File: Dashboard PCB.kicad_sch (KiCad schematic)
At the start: 42 parts

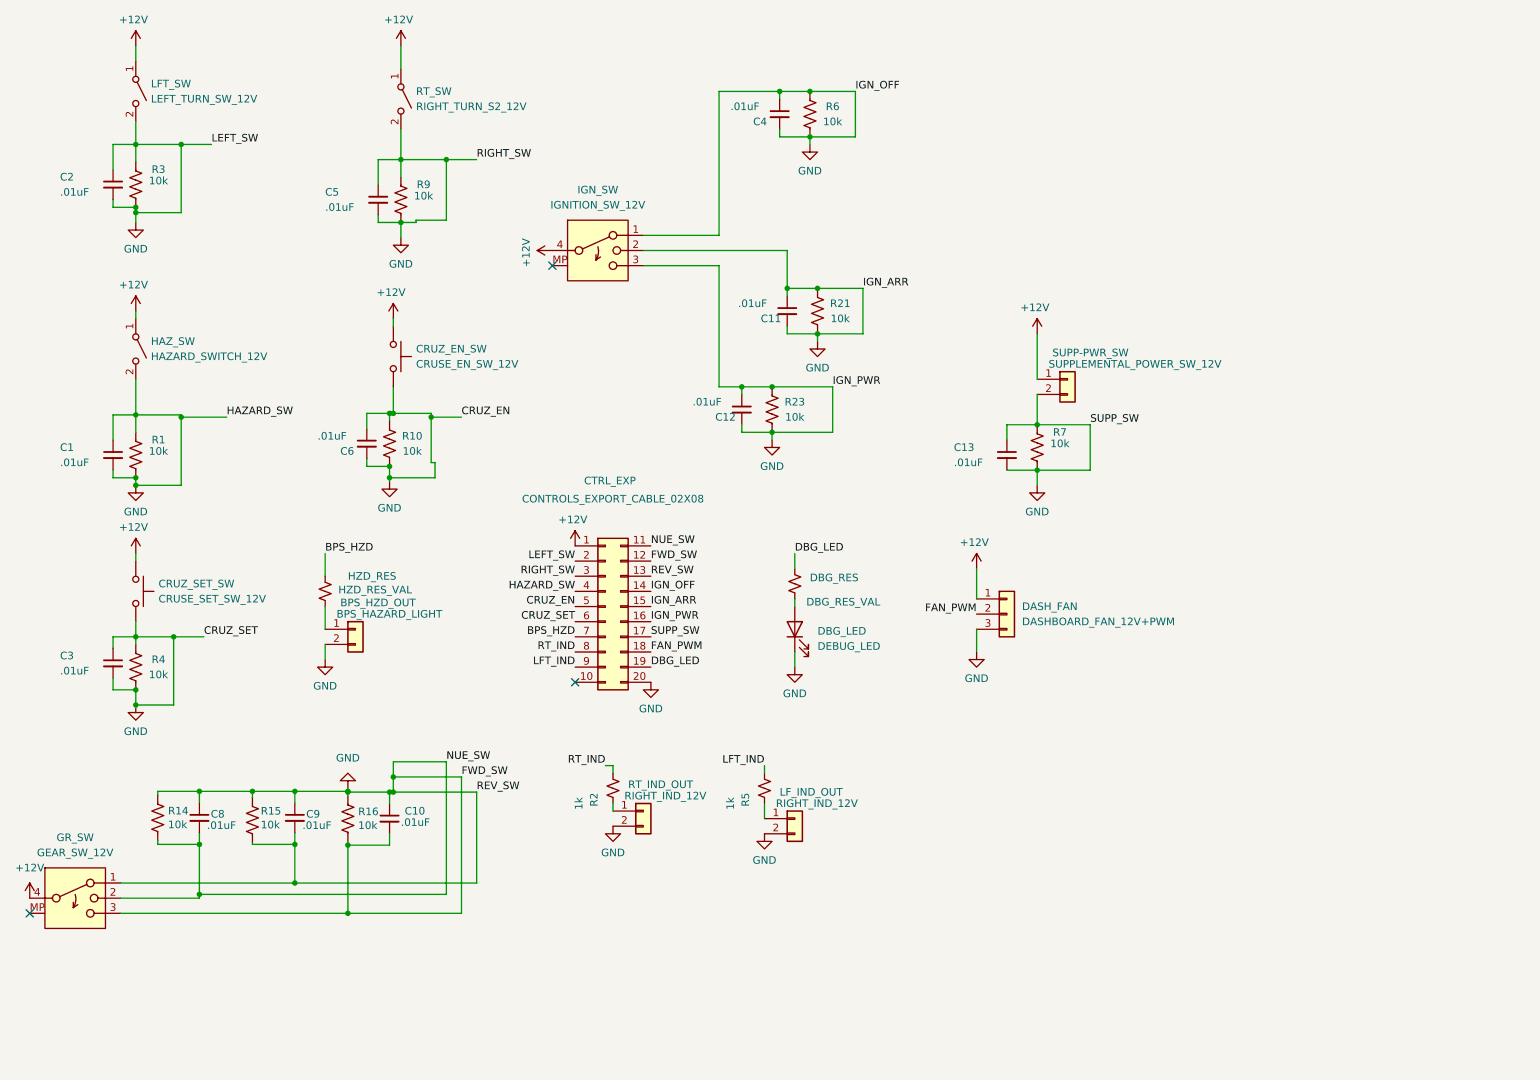
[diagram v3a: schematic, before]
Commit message: Updated dashboard
Took off some unnecessary connections
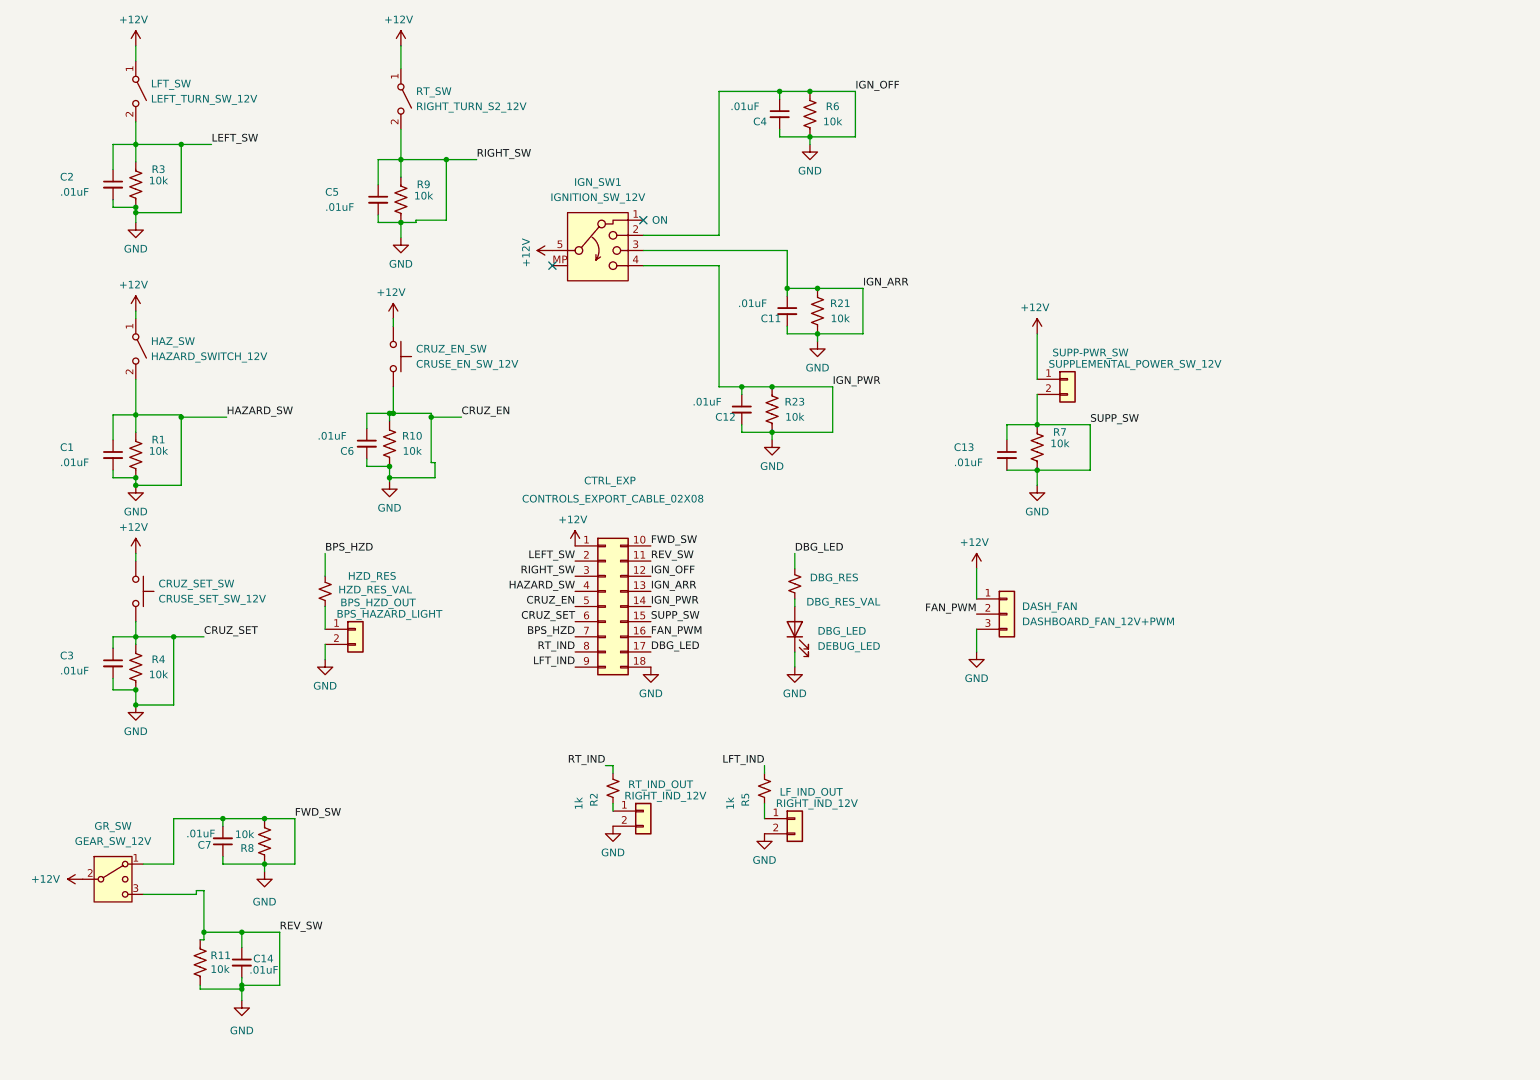
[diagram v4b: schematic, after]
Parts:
- removed C10, C8, C9: .01uF, Capacitor_SMD:C_0805_2012Metric, symbol Device:C_Small
- removed GR_SW: GEAR_SW_12V, symbol Switch:SW_Rotary_1x3_MP
- removed IGN_SW: IGNITION_SW_12V, symbol Switch:SW_Rotary_1x3_MP
- removed R14, R15, R16: 10k, Resistor_SMD:R_0805_2012Metric, symbol Device:R_US
- added C14, C7: .01uF, Capacitor_SMD:C_0805_2012Metric, symbol Device:C_Small
- added GR_SW: GEAR_SW_12V, symbol Switch:SW_SPDT_MSM
- added IGN_SW1: IGNITION_SW_12V, symbol Switch:SW_Rotary_1x4_MP
- added R11, R8: 10k, Resistor_SMD:R_0805_2012Metric, symbol Device:R_US
- CTRL_EXP: symbol Connector_Generic:Conn_02x10_Top_Bottom -> Connector_Generic:Conn_02x09_Top_Bottom
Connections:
- net +12V: now also GR_SW.2 (3), IGN_SW1.5
- net DBG_LED: now also CTRL_EXP.17 (Pin_17); no longer CTRL_EXP.19 (Pin_19)
- net FAN_PWM: now also CTRL_EXP.16 (Pin_16); no longer CTRL_EXP.18 (Pin_18)
- net GND: now also CTRL_EXP.10 (Pin_10), CTRL_EXP.18 (Pin_18), C14.1, C14.2, C7.1, C7.2, GR_SW.1, GR_SW.3 (4), IGN_SW1.2, IGN_SW1.3, IGN_SW1.4, R11.1, R11.2, R8.1, R8.2; no longer CTRL_EXP.16 (Pin_16), CTRL_EXP.17 (Pin_17), CTRL_EXP.20 (Pin_20)
- no-connect marks 3 -> 2
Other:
- note added: "ON"

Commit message: Major redisign
Added a lot of stuff and redesigned a lot of stuff
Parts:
- removed BPS_HZD_OUT: BPS_HAZARD_LIGHT, Connector_Molex:Molex_Micro-Fit_3.0_43650-0215_1x02_P3.00mm_Vertical, symbol Connector_Generic:Conn_01x02
- removed C1, C11, C14, C2, C3, C4, C5, C6, C7: .01uF, Capacitor_SMD:C_0805_2012Metric, symbol Device:C_Small
- removed CRUZ_EN_SW: CRUSE_EN_SW_12V, symbol Switch:SW_Push
- removed CRUZ_SET_SW: CRUSE_SET_SW_12V, symbol Switch:SW_Push
- removed DASH_FAN: DASHBOARD_FAN_12V+PWM, symbol Connector_Generic:Conn_01x03
- removed DBG_LED: DEBUG_LED, symbol Device:LED
- removed DBG_RES: DBG_RES_VAL, Resistor_SMD:R_0805_2012Metric, symbol Device:R_Small_US
- removed GR_SW: GEAR_SW_12V, symbol Switch:SW_SPDT_MSM
- removed HAZ_SW: HAZARD_SWITCH_12V, symbol Switch:SW_SPST
- removed HZD_RES: HZD_RES_VAL, Resistor_SMD:R_0805_2012Metric, symbol Device:R_Small_US
- removed IGN_SW1: IGNITION_SW_12V, symbol Switch:SW_Rotary_1x4_MP
- removed LFT_SW: LEFT_TURN_SW_12V, symbol Switch:SW_SPST
- removed LF_IND_OUT, RT_IND_OUT: RIGHT_IND_12V, Connector_Molex:Molex_Micro-Fit_3.0_43650-0215_1x02_P3.00mm_Vertical, symbol Connector_Generic:Conn_01x02
- removed R1, R10, R11, R21, R23, R3, R4, R6, R7, R8, R9: 10k, Resistor_SMD:R_0805_2012Metric, symbol Device:R_US
- removed R2, R5: 1k, Resistor_SMD:R_0805_2012Metric, symbol Device:R_Small_US
- removed RT_SW: RIGHT_TURN_S2_12V, symbol Switch:SW_SPST
- removed SUPP-PWR_SW: SUPPLEMENTAL_POWER_SW_12V, Connector_Molex:Molex_Micro-Fit_3.0_43650-0215_1x02_P3.00mm_Vertical, symbol Connector_Generic:Conn_01x02
- added BL1: LM555xM, Package_SO:SOIC-8_3.9x4.9mm_P1.27mm, symbol Timer:LM555xM
- added C9: 10uF, Capacitor_SMD:C_0805_2012Metric, symbol Device:C_Small
- added D1: 6.8V, Diode_SMD:D_0805_2012Metric, symbol Device:D_Zener
- added DASH_FAN1: DASHBOARD_FAN_12V+PWM, symbol Connector_Generic:Conn_01x03
- added DBG_LED1: DEBUG_LED, symbol Device:LED
- added DBG_RES1: DBG_RES_VAL, Resistor_SMD:R_0805_2012Metric, symbol Device:R_Small_US
- added R2: 1k, Resistor_SMD:R_0805_2012Metric, symbol Device:R_Small
- added R5: 10k, Resistor_SMD:R_0805_2012Metric, symbol Device:R_Small
- added TP1: LIGHT_CLK, TestPoint:TestPoint_Pad_1.5x1.5mm, symbol Connector:TestPoint
- C13: value .01uF -> 47uF; P/N C0805C103J5RACTU -> C2012X5R0J476M125AC
- CTRL_EXP: symbol Connector_Generic:Conn_02x09_Top_Bottom -> Connector_Generic:Conn_02x07_Top_Bottom
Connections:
- net +12V: now also BL1.4 (R), BL1.8 (VCC), C9.1, DASH_FAN1.1 (Pin_1), R2.1
- net BPS_HZD: now also CTRL_EXP.6 (Pin_6); no longer CTRL_EXP.7 (Pin_7)
- net DBG_LED: now also CTRL_EXP.7 (Pin_7), DBG_RES1.1; no longer CTRL_EXP.17 (Pin_17)
- net FAN_PWM: now also CTRL_EXP.13 (Pin_13), DASH_FAN1.2 (Pin_2); no longer CTRL_EXP.16 (Pin_16)
- net GND: now also BL1.1 (GND), C9.2, D1.2 (A), DASH_FAN1.3 (Pin_3), DBG_LED1.1 (K); no longer C12.1, C13.1, CTRL_EXP.10 (Pin_10), CTRL_EXP.11 (Pin_11), CTRL_EXP.12 (Pin_12), CTRL_EXP.13 (Pin_13), CTRL_EXP.15 (Pin_15), CTRL_EXP.18 (Pin_18), CTRL_EXP.2 (Pin_2), CTRL_EXP.3 (Pin_3), CTRL_EXP.4 (Pin_4), CTRL_EXP.5 (Pin_5), CTRL_EXP.6 (Pin_6)
- net LFT_IND renamed REV_SW
- net RT_IND renamed FWD_SW
- new net: DBG_LED1.2 (A), DBG_RES1.2
- new net: BL1.7 (DIS), R2.2, R5.2
- new net: BL1.5 (CV), C12.1
- new net CRUZ_EN: CTRL_EXP.4 (Pin_4)
- new net CRUZ_SET: CTRL_EXP.5 (Pin_5)
- new net IGN_ARR: CTRL_EXP.11 (Pin_11)
- new net IGN_PWR: CTRL_EXP.12 (Pin_12)
- new net LFT_LIGHTS_OUT: CTRL_EXP.3 (Pin_3)
- new net LIGHT_CLK: BL1.3 (Q), D1.1 (K), TP1.1
- new net RT_LIGHTS_OUT: CTRL_EXP.2 (Pin_2)
- new net SUPP_SW: CTRL_EXP.10 (Pin_10)
- new net TRIGTHRES: BL1.2 (TR), BL1.6 (THR), C13.1, R5.1
- no-connect marks 2 -> 0
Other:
- added sheet Lighting (Lighting.kicad_sch)
- added sheet Switches (Switches.kicad_sch)
- note added: "555 Timer with Rhigh = 1k, Rlow = 10k, C = 47u: ~358ms high, ~325ms low, @1.459Hz"
- note removed: "ON"

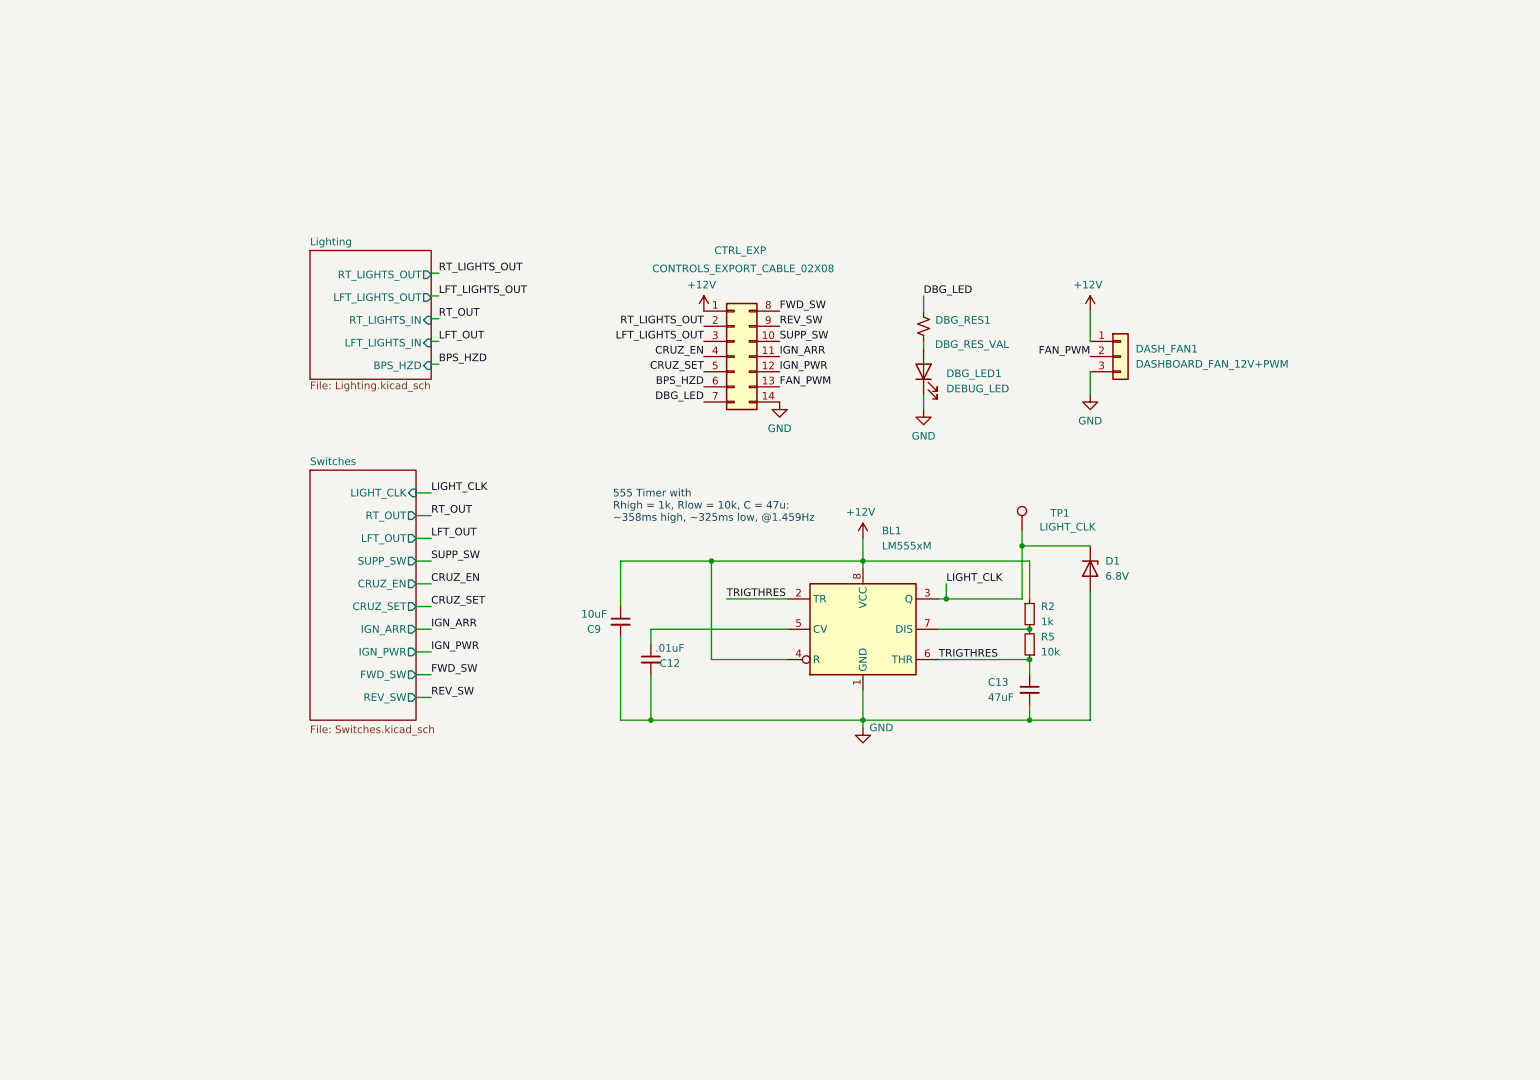
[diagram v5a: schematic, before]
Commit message: Update 1/2
Fixed some of the requested changes.
Still need to fix it up a bit more.
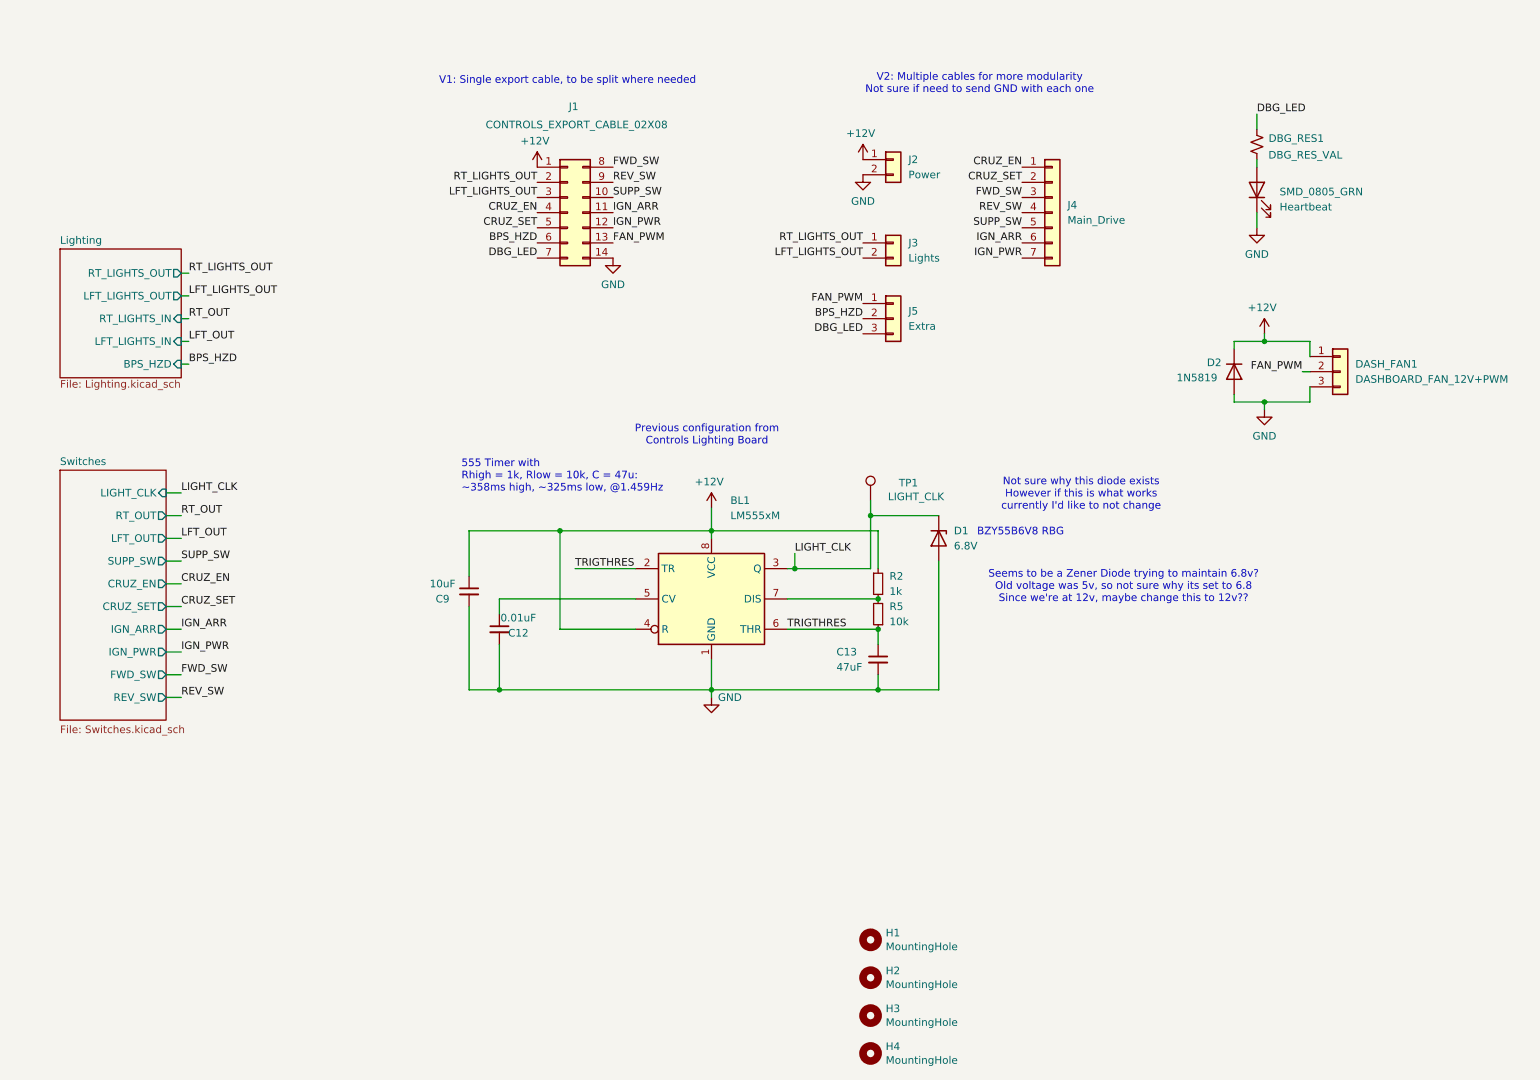
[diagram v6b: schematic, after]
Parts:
- added D2: 1N5819, symbol Device:D
- added H1, H2, H3, H4: MountingHole, MountingHole:MountingHole_3mm, symbol Mechanical:MountingHole
- added J2: Power, symbol Connector_Generic:Conn_01x02
- added J3: Lights, symbol Connector_Generic:Conn_01x02
- added J4: Main_Drive, symbol Connector_Generic:Conn_01x07
- added J5: Extra, symbol Connector_Generic:Conn_01x03
- C12: value .01uF -> 0.01uF
- SMD_0805_GRN: renamed from DBG_LED1; value DEBUG_LED -> Heartbeat
- renumbered CTRL_EXP to J1
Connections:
- net +12V: now also D2.1 (K), J2.1 (Pin_1)
- net BPS_HZD: now also J5.2 (Pin_2)
- net CRUZ_EN: now also J4.1 (Pin_1)
- net CRUZ_SET: now also J4.2 (Pin_2)
- net DBG_LED: now also J5.3 (Pin_3)
- net FAN_PWM: now also J5.1 (Pin_1)
- net FWD_SW: now also J4.3 (Pin_3)
- net GND: now also D2.2 (A), J2.2 (Pin_2)
- net IGN_ARR: now also J4.6 (Pin_6)
- net IGN_PWR: now also J4.7 (Pin_7)
- net LFT_LIGHTS_OUT: now also J3.2 (Pin_2)
- net REV_SW: now also J4.4 (Pin_4)
- net RT_LIGHTS_OUT: now also J3.1 (Pin_1)
- net SUPP_SW: now also J4.5 (Pin_5)
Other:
- note added: "BZY55B6V8 RBG"
- note added: "Not sure why this diode exists However if this is what works currently I'd like to not change"
- note added: "Previous configuration from Controls Lighting Board"
- note added: "Seems to be a Zener Diode trying to maintain 6.8v? Old voltage was 5v, so not sure why its set to 6.8 Since we're at 12v, maybe change this to 12v??"
- note added: "V1: Single export cable, to be split where needed"
- note added: "V2: Multiple cables for more modularity Not sure if need to send GND with each one"
- moved on the sheet: BL1, C12, C13, C9, D1, DASH_FAN1, DBG_RES1, J1, R2, R5, SMD_0805_GRN, TP1
